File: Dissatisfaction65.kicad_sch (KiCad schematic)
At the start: 139 parts, among them U1 Pro_Micro_ProMicro

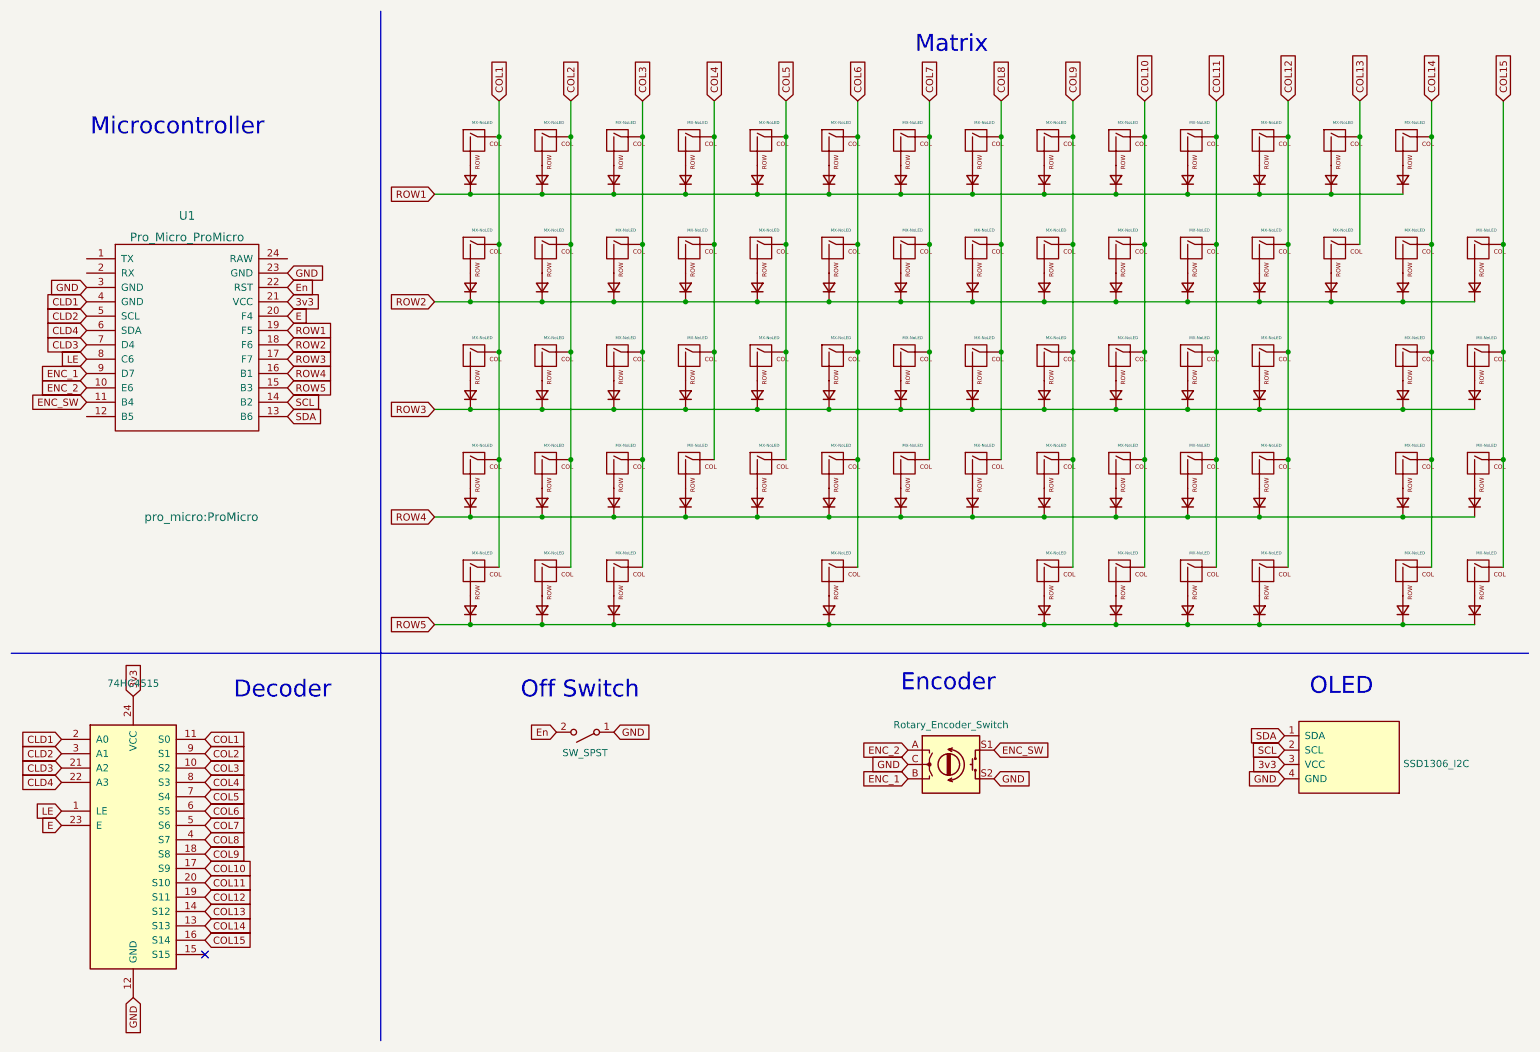
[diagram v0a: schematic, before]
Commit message: Placed NICE!-nano such that the micro usb comes right up to the edge of the board re-routed a bunch of column signals, the rotary encoder signals, reset switch, rotary encoder push button switch, 3v3, I2C signals, and gnd NICE!-nano should be encorporated now but should probably double check everything. DRC has two warnings about silkscreen getting clipped but there's nothing we can really do because the NICE-nano doesn't really fit anywhere else. Updated DRC constraints for JLCPCB fab. Should double check Added Circuit-Dude logo because I am circuit-dude and I did the layout and Thomas can't stop me unless he learns how to do layout.
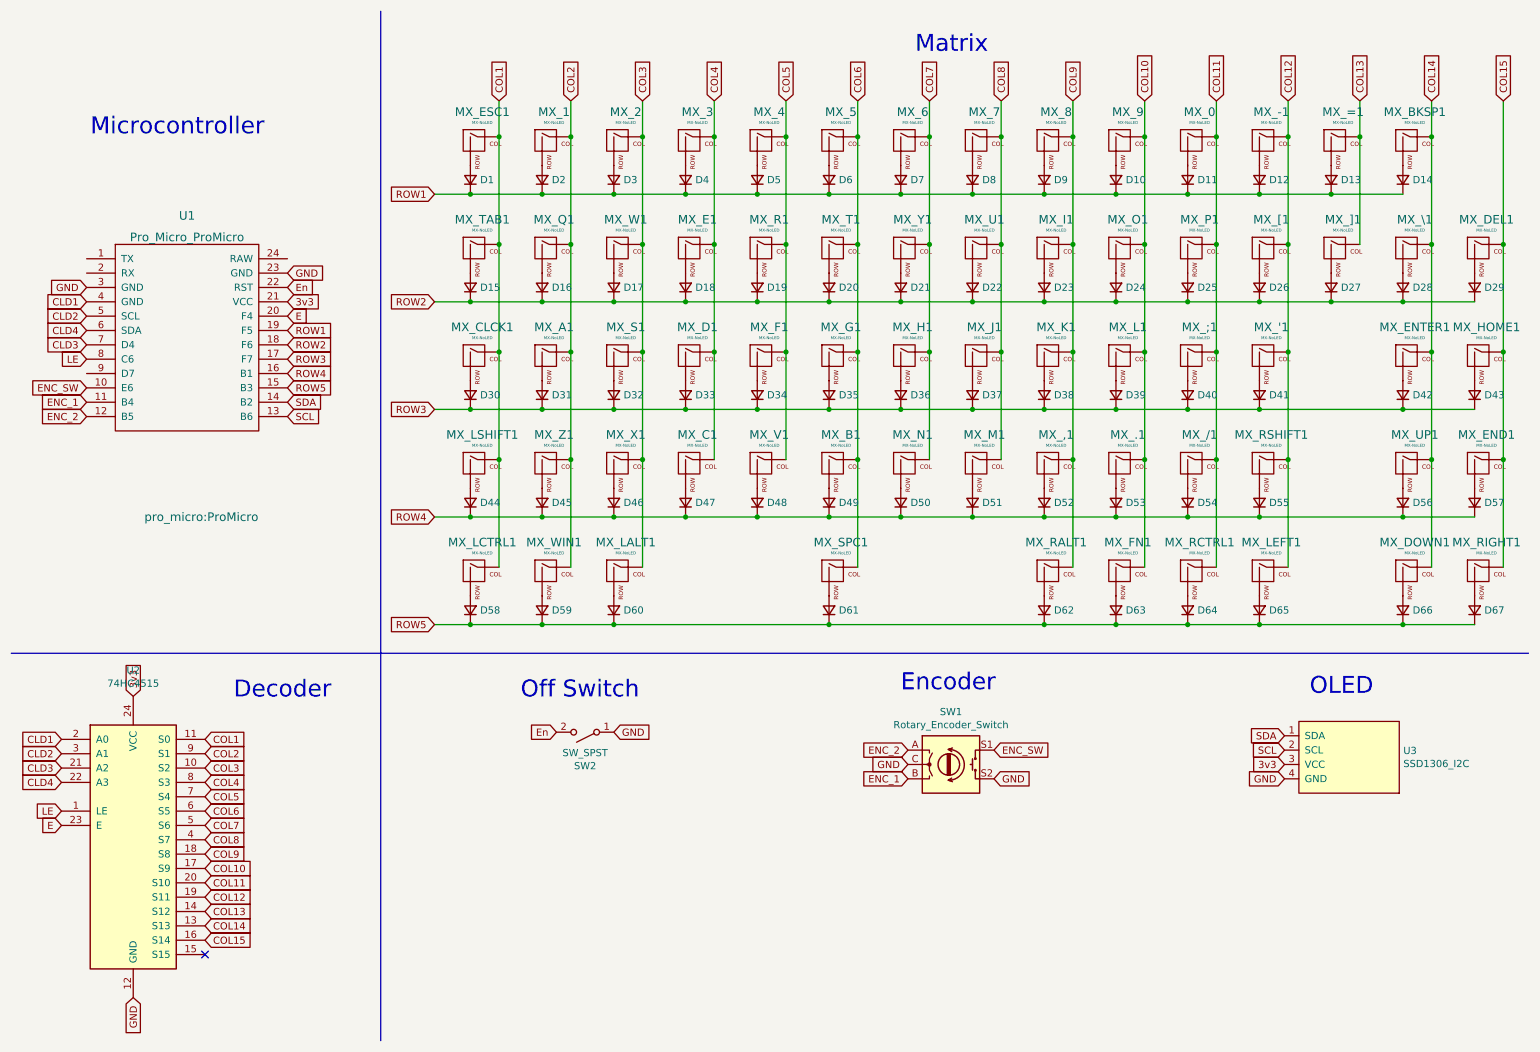
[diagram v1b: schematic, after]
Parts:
- gave numbers to parts that had none: 138
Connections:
- net ENC_1: now also U1.11 (B4); no longer U1.9 (D7)
- net ENC_2: now also U1.12 (B5); no longer U1.10 (E6)
- net ENC_SW: now also U1.10 (E6); no longer U1.11 (B4)
- net SCL: now also U1.13 (B6); no longer U1.14 (B2)
- net SDA: now also U1.14 (B2); no longer U1.13 (B6)
